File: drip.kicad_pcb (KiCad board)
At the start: 2 copper layers, 119.4 x 107.9 mm, 88 parts, among them J1 ISP, J2 2xAA Battery Holder, Q1 2n2907, Q2 2n2907, Q3 2n2907, Q4 2n2907, Q5 2n2907, Q6 2n2907, Q7 2n2907, Q8 2n2907, Q9 2n2222, SW1 Bin, SW10 Recall, SW11 D, SW12 A, SW13 7, SW14 4, SW15 1, SW16 0, SW17 Hex, SW18 E, SW19 B, SW2 Store, SW20 8, SW21 5, SW22 2, SW23 Decimal, SW24 Oct, SW25 F, SW26 C, SW27 9, SW28 6, SW29 3, SW3 Shift, SW30 +/-, SW31 Clear, SW32 K, SW33 Div, SW34 Mul, SW35 Minus, SW36 Plus, SW37 Enter, SW4 1'sCompl, SW5 Or, SW6 And, SW7 Xor, SW8 Clear Entry, SW9 Dec, U1 74HC138, U2 5641AS-4Digit-7Segment, U3 5641AS-4Digit-7Segment, U4 MSP430G2553IN20, U5 74HC251, U6 74HC138, U7 74HC595, U8 XC6372A331PR-G

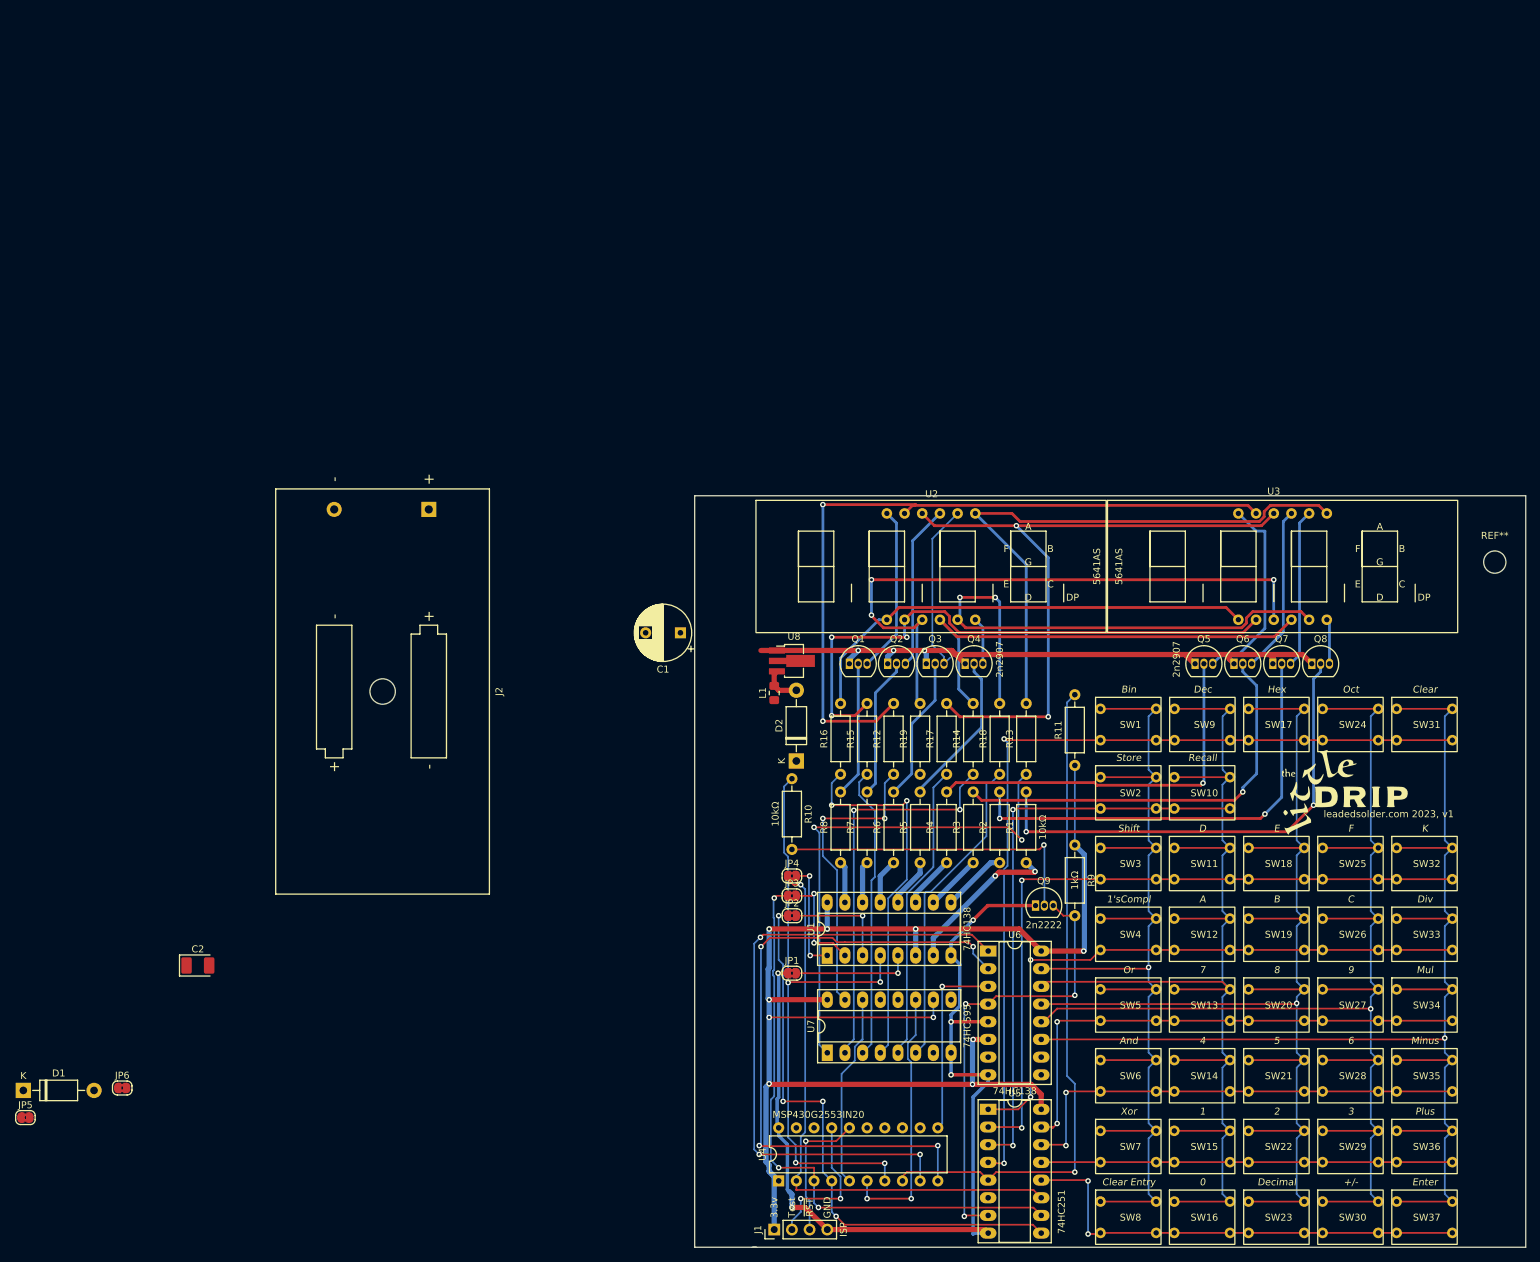
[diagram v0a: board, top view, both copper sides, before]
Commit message: layout complete, lots of warnings
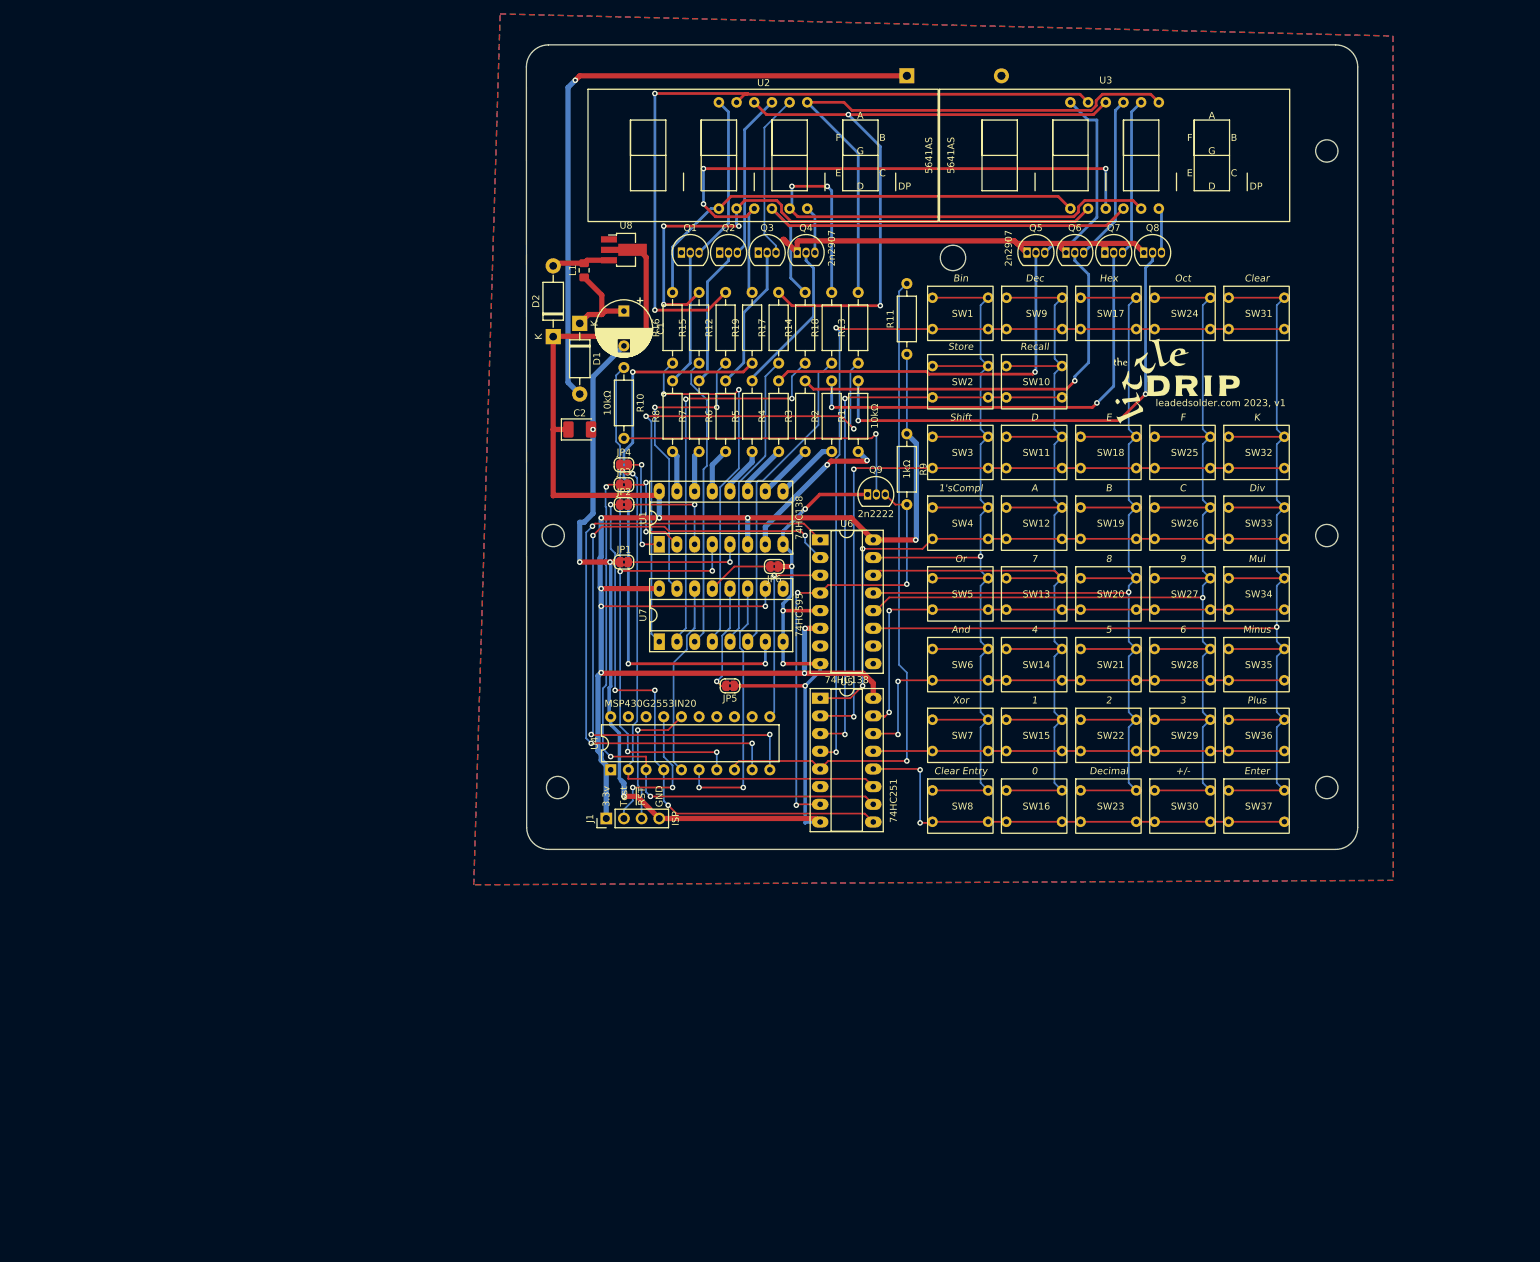
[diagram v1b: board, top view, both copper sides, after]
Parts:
- removed the REF** at (225.4, 101.0)
- added REF**: MountingHole_3.2mm_M3_DIN965, MountingHole:MountingHole_3.2mm_M3_DIN965, F.Cu at (90.8, 133.3)
- added REF**: MountingHole_3.2mm_M3_DIN965, MountingHole:MountingHole_3.2mm_M3_DIN965, F.Cu at (201.3, 133.3)
- added REF**: MountingHole_3.2mm_M3_DIN965, MountingHole:MountingHole_3.2mm_M3_DIN965, F.Cu at (201.3, 41.9)
- added REF**: MountingHole_3.2mm_M3_DIN965, MountingHole:MountingHole_3.2mm_M3_DIN965, F.Cu at (201.3, 97.2)
- added REF**: MountingHole_3.2mm_M3_DIN965, MountingHole:MountingHole_3.2mm_M3_DIN965, F.Cu at (90.2, 97.2)
- J2: moved to B.Cu
- moved D1 136.1 mm to (94.0, 66.7), turned to -90 degrees
- moved JP6 119.9 mm to (121.9, 101.6), turned to 180 degrees
- moved JP5 118.7 mm to (115.6, 118.7), turned to 180 degrees
- moved C2 94.5 mm to (94.0, 81.9)
- moved J2 92.7 mm to (141.0, 31.1)
- moved D2 70.3 mm to (90.2, 68.6)
- moved L1 66.6 mm to (94.6, 59.1)
- moved Q9 63.8 mm to (135.3, 91.3)
- moved SW27 63.8 mm to (176.6, 103.3)
- moved SW28 63.8 mm to (176.6, 113.4)
- moved SW29 63.8 mm to (176.6, 123.6)
- moved SW30 63.8 mm to (176.6, 133.8)
- moved G*** 63.8 mm to (179.7, 74.9)
- moved J1 63.8 mm to (97.8, 137.8)
- moved JP1 63.8 mm to (100.3, 101.0)
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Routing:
- net /AA_POSITIVE: track 0.00 -> 94.1 mm, vias 0 -> 1
- net /LED_DP: track 0.00 -> 83.2 mm, vias 0 -> 3
- net VCC: track 212.3 -> 282.3 mm
- net GND: track 231.9 -> 249.9 mm, vias 8 -> 9
- net Net-(JP5-Pad2): track 0.00 -> 15.7 mm, vias 0 -> 1
- net /3.0v: track 0.00 -> 13.5 mm
- net Net-(JP6-Pad2): track 0.00 -> 9.56 mm
- net Net-(D2-Pad2): track 5.68 -> 8.35 mm
- net Net-(Q3-Pad3): track 25.0 -> 23.8 mm
- added copper zone on B.Cu, net GND
- added copper zone on F.Cu, net GND
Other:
- board size 119.4 x 107.9 mm -> 119.4 x 115.6 mm

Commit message: Test hooks
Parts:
- added REF**: MountingHole_3.2mm_M3_DIN965, MountingHole:MountingHole_3.2mm_M3_DIN965, F.Cu at (90.2, 41.9)
- added TP1: 3.3v, TestPoint:TestPoint_Loop_D2.50mm_Drill1.85mm, F.Cu at (90.8, 107.3)
- added TP2: GND, TestPoint:TestPoint_Loop_D2.50mm_Drill1.85mm, F.Cu at (90.8, 112.8)
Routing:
- net VCC: track 282.3 -> 288.6 mm
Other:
- board text added: "math is hard"

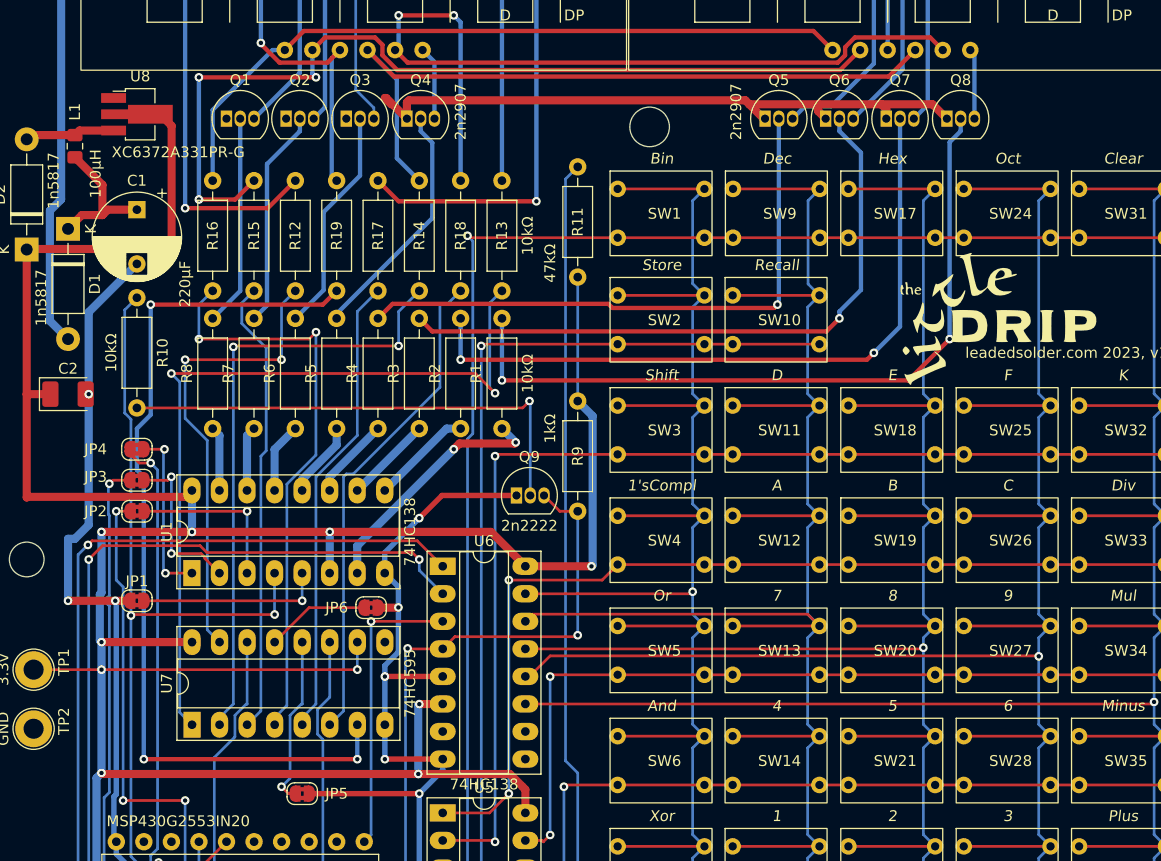
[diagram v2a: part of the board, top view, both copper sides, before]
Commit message: Silkscreen warnings dealt with
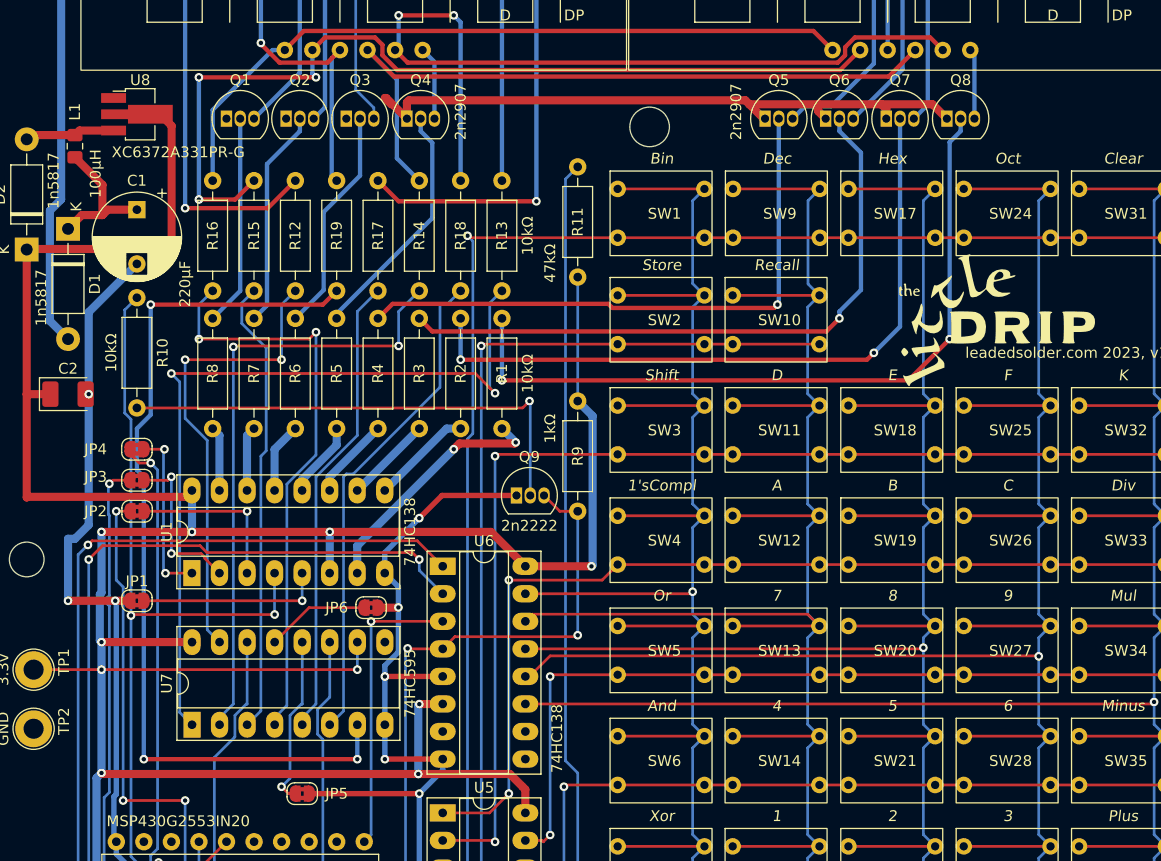
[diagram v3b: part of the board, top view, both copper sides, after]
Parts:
- moved G*** 0.18 mm to (179.6, 75.1)
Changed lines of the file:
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@@
     (property "Sheetname" "")
     (attr through_hole)
-    (fp_text reference "R1" (at 5.08 -2.37 90) (layer "F.SilkS")
+    (fp_text reference "R1" (at 5.08 0 90) (layer "F.SilkS")
       (effects (font (size 1 1) (thickness 0.15)))
     )
@@
     (property "Sheetname" "")
     (attr through_hole)
-    (fp_text reference "R3" (at 5.08 -2.37 90) (layer "F.SilkS")
+    (fp_text reference "R3" (at 5.08 0 90) (layer "F.SilkS")
       (effects (font (size 1 1) (thickness 0.15)))
     )
@@
       (effects (font (size 1 1) (thickness 0.15)))
     )
-    (fp_text user "K" (at 0 -2.1 90) (layer "F.SilkS")
+    (fp_text user "K" (at -2.032 -0.762 90) (layer "F.SilkS")
       (effects (font (size 1 1) (thickness 0.15)))
     )
@@
   )
   (footprint "Logos:little-drip-tiny" (layer "F.Cu")
-    (at 179.705 74.93)
+    (at 179.578 75.057)
     (attr board_only exclude_from_pos_files exclude_from_bom)
     (fp_text reference "G***" (at 0 0) (layer "F.SilkS") hide
@@
     (property "Sheetname" "")
     (attr through_hole)
-    (fp_text reference "R7" (at 5.08 -2.37 90) (layer "F.SilkS")
+    (fp_text reference "R7" (at 5.08 0 90) (layer "F.SilkS")
       (effects (font (size 1 1) (thickness 0.15)))
     )
@@
     (property "Sheetname" "")
     (attr smd)
-    (fp_text reference "U8" (at 0.3 -3.5) (layer "F.SilkS")
+    (fp_text reference "U8" (at 0.3 -3.151) (layer "F.SilkS")
       (effects (font (size 1 1) (thickness 0.15)))
     )
@@
     (property "Sheetname" "")
     (attr through_hole)
-    (fp_text reference "R2" (at 5.08 -2.37 90) (layer "F.SilkS")
+    (fp_text reference "R2" (at 5.08 0 90) (layer "F.SilkS")
       (effects (font (size 1 1) (thickness 0.15)))
     )
@@
     (property "Sheetname" "")
     (attr through_hole)
-    (fp_text reference "R6" (at 5.08 -2.37 90) (layer "F.SilkS")
+    (fp_text reference "R6" (at 5.08 0 90) (layer "F.SilkS")
       (effects (font (size 1 1) (thickness 0.15)))
     )
@@
     (property "Sheetname" "")
     (attr through_hole)
-    (fp_text reference "R5" (at 5.08 -2.37 90) (layer "F.SilkS")
+    (fp_text reference "R5" (at 5.08 0 90) (layer "F.SilkS")
       (effects (font (size 1 1) (thickness 0.15)))
     )
@@
       (effects (font (size 1 1) (thickness 0.15)))
     )
-    (fp_text value "74HC138" (at 3.81 20.11) (layer "F.SilkS")
+    (fp_text value "74HC138" (at 10.541 15.885 90) (layer "F.SilkS")
       (effects (font (size 1 1) (thickness 0.15)))
     )
@@
     (property "Sheetname" "")
     (attr through_hole)
-    (fp_text reference "R8" (at 5.08 -2.37 90) (layer "F.SilkS")
+    (fp_text reference "R8" (at 5.08 0 90) (layer "F.SilkS")
       (effects (font (size 1 1) (thickness 0.15)))
     )
@@
     (property "Sheetname" "")
     (attr through_hole)
-    (fp_text reference "R4" (at 5.08 -2.37 90) (layer "F.SilkS")
+    (fp_text reference "R4" (at 5.08 0 90) (layer "F.SilkS")
       (effects (font (size 1 1) (thickness 0.15)))
     )

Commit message: Mode LEDs
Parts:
- added D3: LED, LED_SMD:LED_0805_2012Metric_Pad1.15x1.40mm_HandSolder, F.Cu at (161.7, 60.3)
- added D4: LED, LED_SMD:LED_0805_2012Metric_Pad1.15x1.40mm_HandSolder, F.Cu at (182.6, 60.3)
- added D5: LED, LED_SMD:LED_0805_2012Metric_Pad1.15x1.40mm_HandSolder, F.Cu at (171.8, 60.3)
- added D6: LED, LED_SMD:LED_0805_2012Metric_Pad1.15x1.40mm_HandSolder, F.Cu at (151.1, 60.3)
- added R20: 1kΩ, Resistor_SMD:R_0805_2012Metric_Pad1.20x1.40mm_HandSolder, F.Cu at (187.3, 56.5)
- added R21: 1kΩ, Resistor_SMD:R_0805_2012Metric_Pad1.20x1.40mm_HandSolder, F.Cu at (187.3, 54.0)
- added R22: 1kΩ, Resistor_SMD:R_0805_2012Metric_Pad1.20x1.40mm_HandSolder, F.Cu at (183.2, 54.0)
- added R23: 1kΩ, Resistor_SMD:R_0805_2012Metric_Pad1.20x1.40mm_HandSolder, F.Cu at (183.2, 56.5)
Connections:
- U4 pad 12: unconnected-(U4-Pad12) -> /DEC_LED
- U4 pad 13: unconnected-(U4-Pad13) -> /OCT_LED
- U4 pad 18: unconnected-(U4-Pad18) -> /BIN_LED
- U4 pad 19: unconnected-(U4-Pad19) -> /HEX_LED
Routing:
- net /HEX_LED: track 0.00 -> 149.9 mm, vias 0 -> 5
- net /OCT_LED: track 0.00 -> 126.4 mm, vias 0 -> 2
- net /BIN_LED: track 0.00 -> 113.4 mm, vias 0 -> 3
- net /DEC_LED: track 0.00 -> 107.1 mm, vias 0 -> 3
- net Net-(D6-Pad1): track 0.00 -> 33.4 mm
- net Net-(D3-Pad1): track 0.00 -> 28.8 mm
- net Net-(D5-Pad1): track 0.00 -> 12.0 mm
- net Net-(D4-Pad1): track 0.00 -> 8.49 mm
- net GND: track 249.9 -> 254.6 mm
